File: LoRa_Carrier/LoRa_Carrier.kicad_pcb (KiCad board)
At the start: 4 copper layers, 80.5 x 56.9 mm, 12 parts, among them J1 Conn_01x07_Pin, J2 Conn_01x07_Pin, J3 Conn_01x02_Pin, U1 RA-08H(915), U2 BWU.FL-IPEX1, U3 AMS1117-3.3_C347222

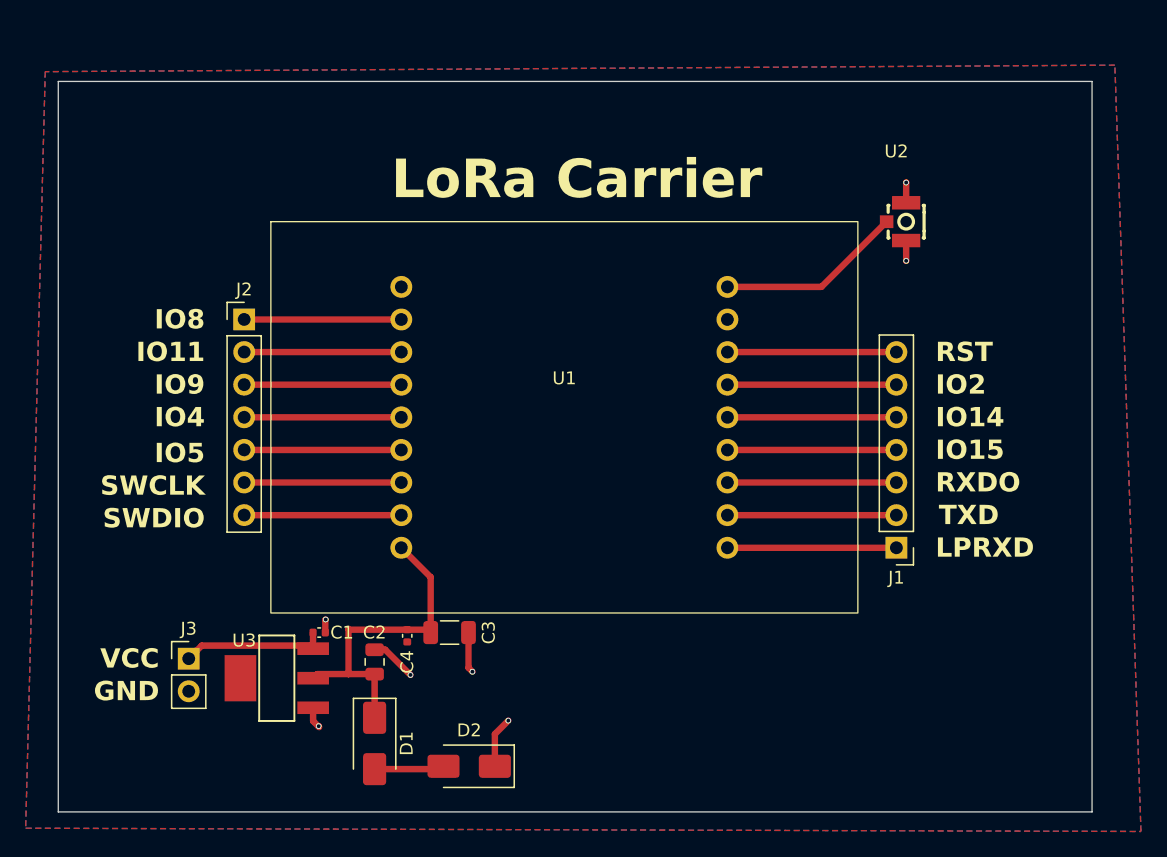
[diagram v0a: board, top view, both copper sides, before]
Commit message: Reworked Lora Carrier.
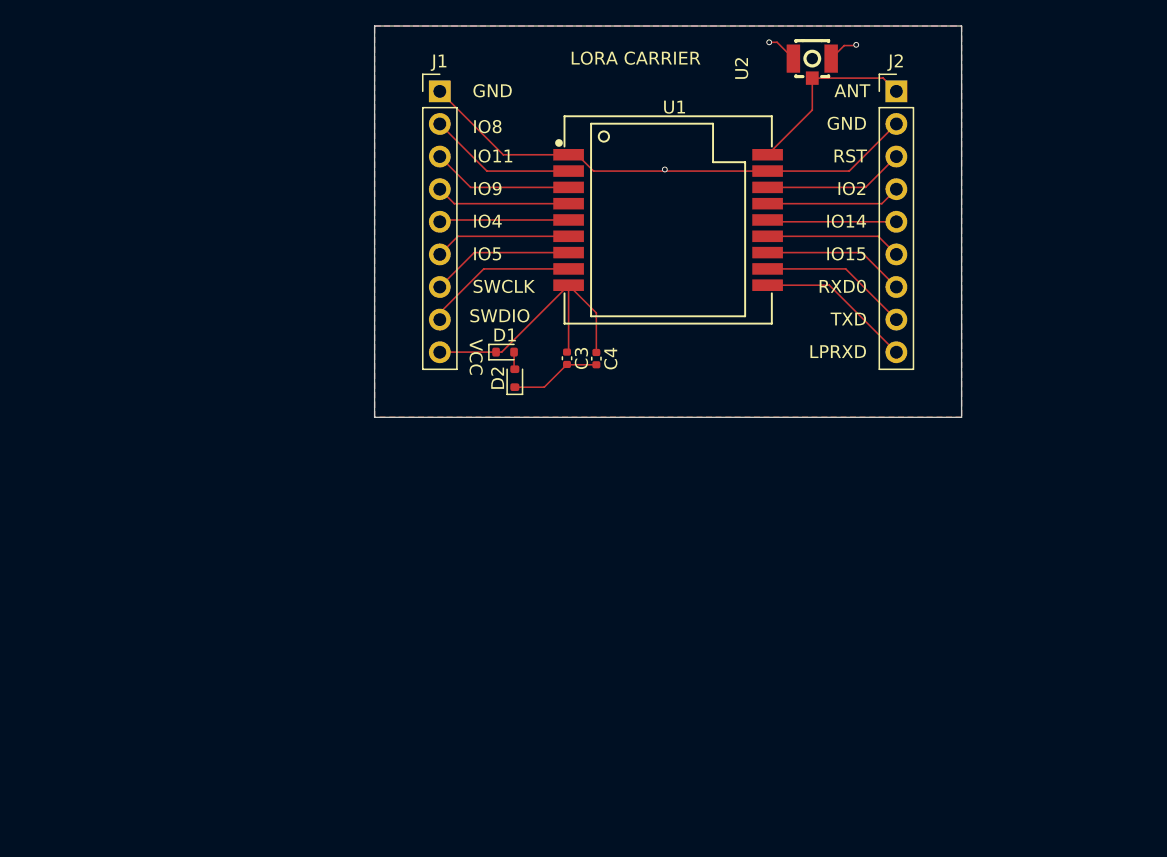
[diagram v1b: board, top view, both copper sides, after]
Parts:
- removed C1: 10uF, Capacitor_SMD:C_0402_1005Metric
- removed C2: 22uF, Capacitor_SMD:C_0805_2012Metric
- removed J3: Conn_01x02_Pin, Connector_PinHeader_2.54mm:PinHeader_1x02_P2.54mm_Vertical
- removed U3: AMS1117-3.3_C347222, PARTS:SOT-223-4_L6.5-W3.5-P2.30-LS7.0-BR
- C3: footprint Capacitor_SMD:C_1206_3216Metric -> Capacitor_SMD:C_0402_1005Metric
- D1, D2: footprint Diode_SMD:D_SMA -> Diode_SMD:D_SOD-523
- J1, J2: value Conn_01x07_Pin -> Conn_01x09_Pin; footprint Connector_PinHeader_2.54mm:PinHeader_1x07_P2.54mm_Vertical -> Connector_PinHeader_2.54mm:PinHeader_1x09_P2.54mm_Vertical
- U1: footprint PARTS:RA_08H-BREAKOUT -> PARTS:COMM-SMD_18P-L16.0-W16.0-P1.27-BL_RA-08H
- moved J2 53.8 mm to (188.0, 58.4)
- moved J1 50.3 mm to (152.4, 58.4), turned to 0 degrees
- moved D1 32.1 mm to (157.5, 78.7), turned to 0 degrees
- moved D2 30.4 mm to (158.2, 80.8), turned to 90 degrees
- moved C4 26.1 mm to (164.6, 79.2)
- moved C3 23.2 mm to (162.3, 79.2), turned to -90 degrees
- moved U1 15.2 mm to (170.2, 68.5), turned to -90 degrees
- moved U2 13.6 mm to (181.4, 56.6), turned to 90 degrees
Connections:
- C3 pad 1: +3.3V -> /VCC
- C4 pad 1: +3.3V -> /VCC
- D1 pad 1: +3.3V -> /VCC
- J1 pad 1: Net-(J1-Pin_1) -> GND
- J1 pad 2: Net-(J1-Pin_2) -> /IO8
- J1 pad 3: Net-(J1-Pin_3) -> /IO11
- J1 pad 4: Net-(J1-Pin_4) -> /IO9
- J1 pad 5: Net-(J1-Pin_5) -> /IO4
- J1 pad 6: Net-(J1-Pin_6) -> /IO5
- J1 pad 7: Net-(J1-Pin_7) -> /SWCLK
- J2 pad 1: Net-(J2-Pin_1) -> /ANT
- J2 pad 2: Net-(J2-Pin_2) -> GND
- J2 pad 3: Net-(J2-Pin_3) -> /RST
- J2 pad 4: Net-(J2-Pin_4) -> /IO2
- J2 pad 5: Net-(J2-Pin_5) -> /IO14
- J2 pad 6: Net-(J2-Pin_6) -> /IO15
- J2 pad 7: Net-(J2-Pin_7) -> /RXD0
- U1 pad 10: Net-(J1-Pin_1) -> /LPRXD
- U1 pad 11: Net-(J1-Pin_2) -> /TXD
- U1 pad 12: Net-(J1-Pin_3) -> /RXD0
- U1 pad 13: Net-(J1-Pin_4) -> /IO15
- U1 pad 14: Net-(J1-Pin_5) -> /IO14
- U1 pad 15: Net-(J1-Pin_6) -> /IO2
- U1 pad 16: Net-(J1-Pin_7) -> /RST
- U1 pad 18: Net-(U1-ANT) -> /ANT
- U1 pad 2: Net-(J2-Pin_1) -> /IO8
- U1 pad 3: Net-(J2-Pin_2) -> /IO11
- U1 pad 4: Net-(J2-Pin_3) -> /IO9
- U1 pad 5: Net-(J2-Pin_4) -> /IO4
- U1 pad 6: Net-(J2-Pin_5) -> /IO5
- U1 pad 7: Net-(J2-Pin_6) -> /SWCLK
- U1 pad 8: Net-(J2-Pin_7) -> /SWDIO
- U1 pad 9: +3.3V -> /VCC
- U2 pad 1: Net-(U1-ANT) -> /ANT
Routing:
- net GND: track 16.7 -> 51.7 mm, vias 7 -> 3
- net +3.3V: track 25.9 -> 0.00 mm
- net /VCC: track 0.00 -> 23.6 mm
- net Net-(U1-ANT): track 14.5 -> 0.00 mm
- net /ANT: track 0.00 -> 14.4 mm
- net Net-(J1-Pin_7): track 13.2 -> 0.00 mm
- net Net-(J1-Pin_6): track 13.2 -> 0.00 mm
- net Net-(J1-Pin_5): track 13.2 -> 0.00 mm
- net Net-(J1-Pin_4): track 13.2 -> 0.00 mm
- net Net-(J1-Pin_3): track 13.2 -> 0.00 mm
- net Net-(J1-Pin_2): track 13.2 -> 0.00 mm
- net Net-(J1-Pin_1): track 13.2 -> 0.00 mm
- net Net-(J2-Pin_6): track 12.2 -> 0.00 mm
- net Net-(J2-Pin_1): track 12.2 -> 0.00 mm
- net Net-(J2-Pin_7): track 12.2 -> 0.00 mm
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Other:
- board size 80.5 x 56.9 mm -> 45.7 x 30.5 mm
- board text added: "ANT"
- board text added: "LORA CARRIER"
- board text added: "RXD0"
- board text removed: "LoRa Carrier"
- board text removed: "RXDO"
